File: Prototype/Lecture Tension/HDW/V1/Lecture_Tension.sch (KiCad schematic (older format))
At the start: 5 parts

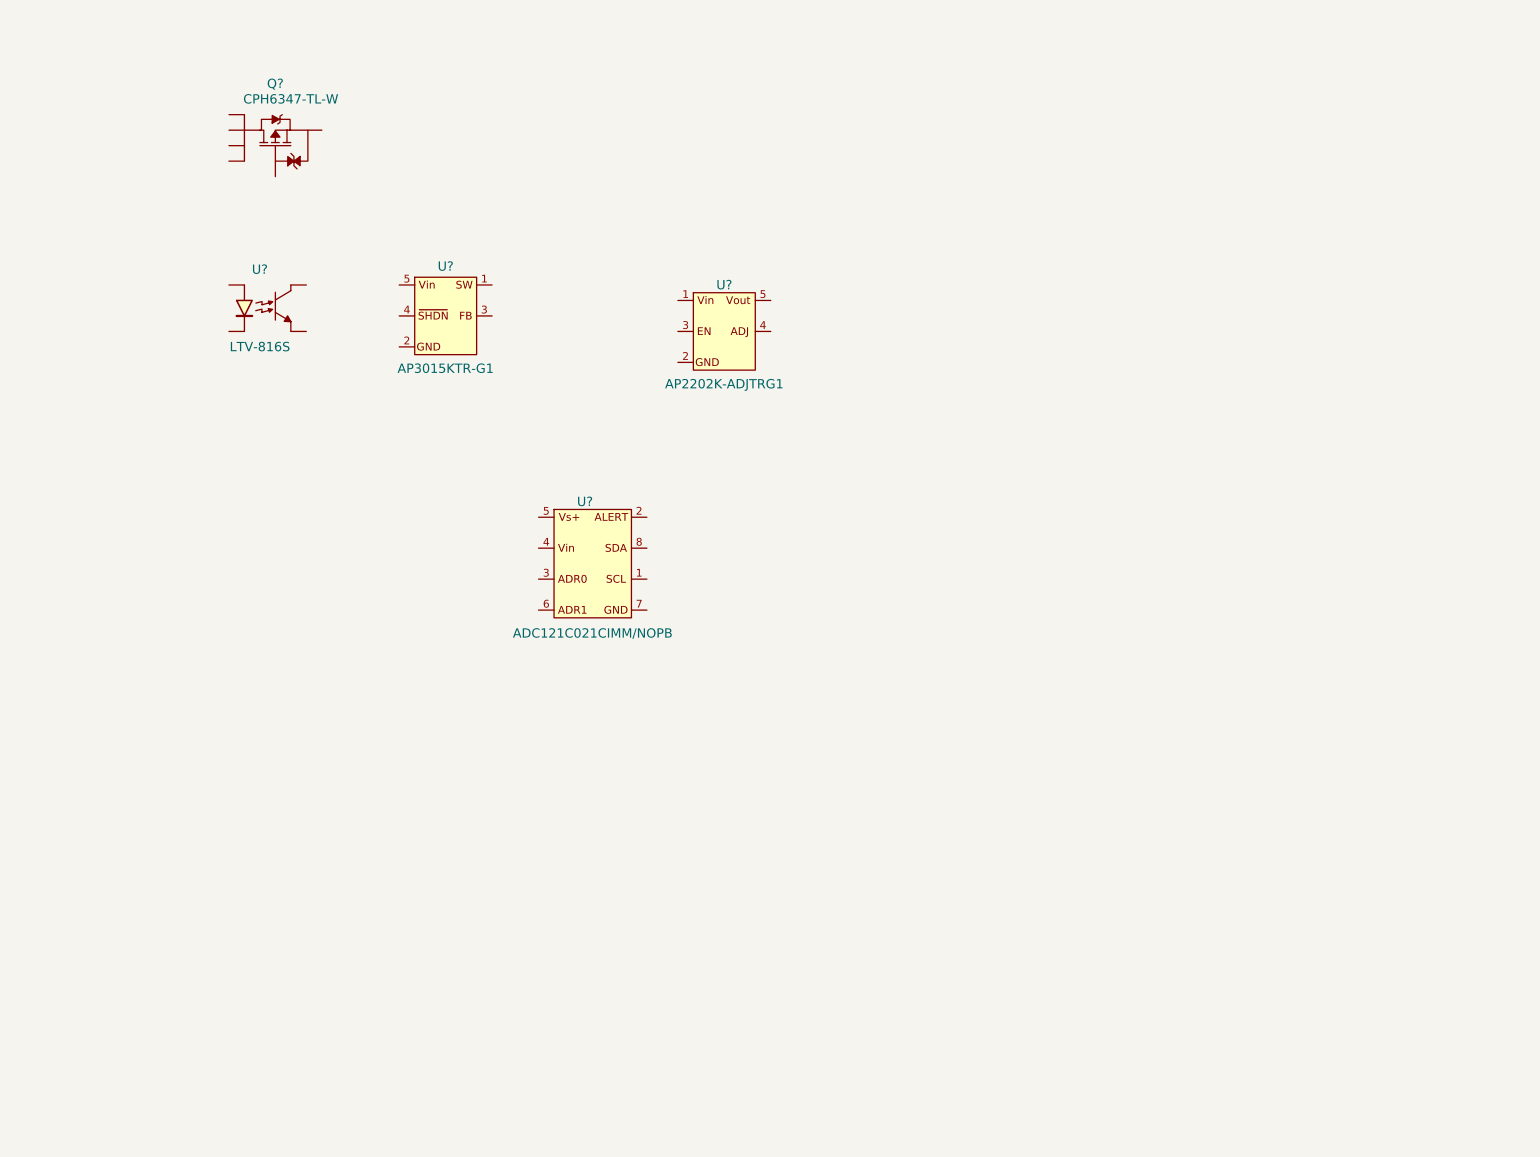
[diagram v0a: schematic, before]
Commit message: SCH ADC part done
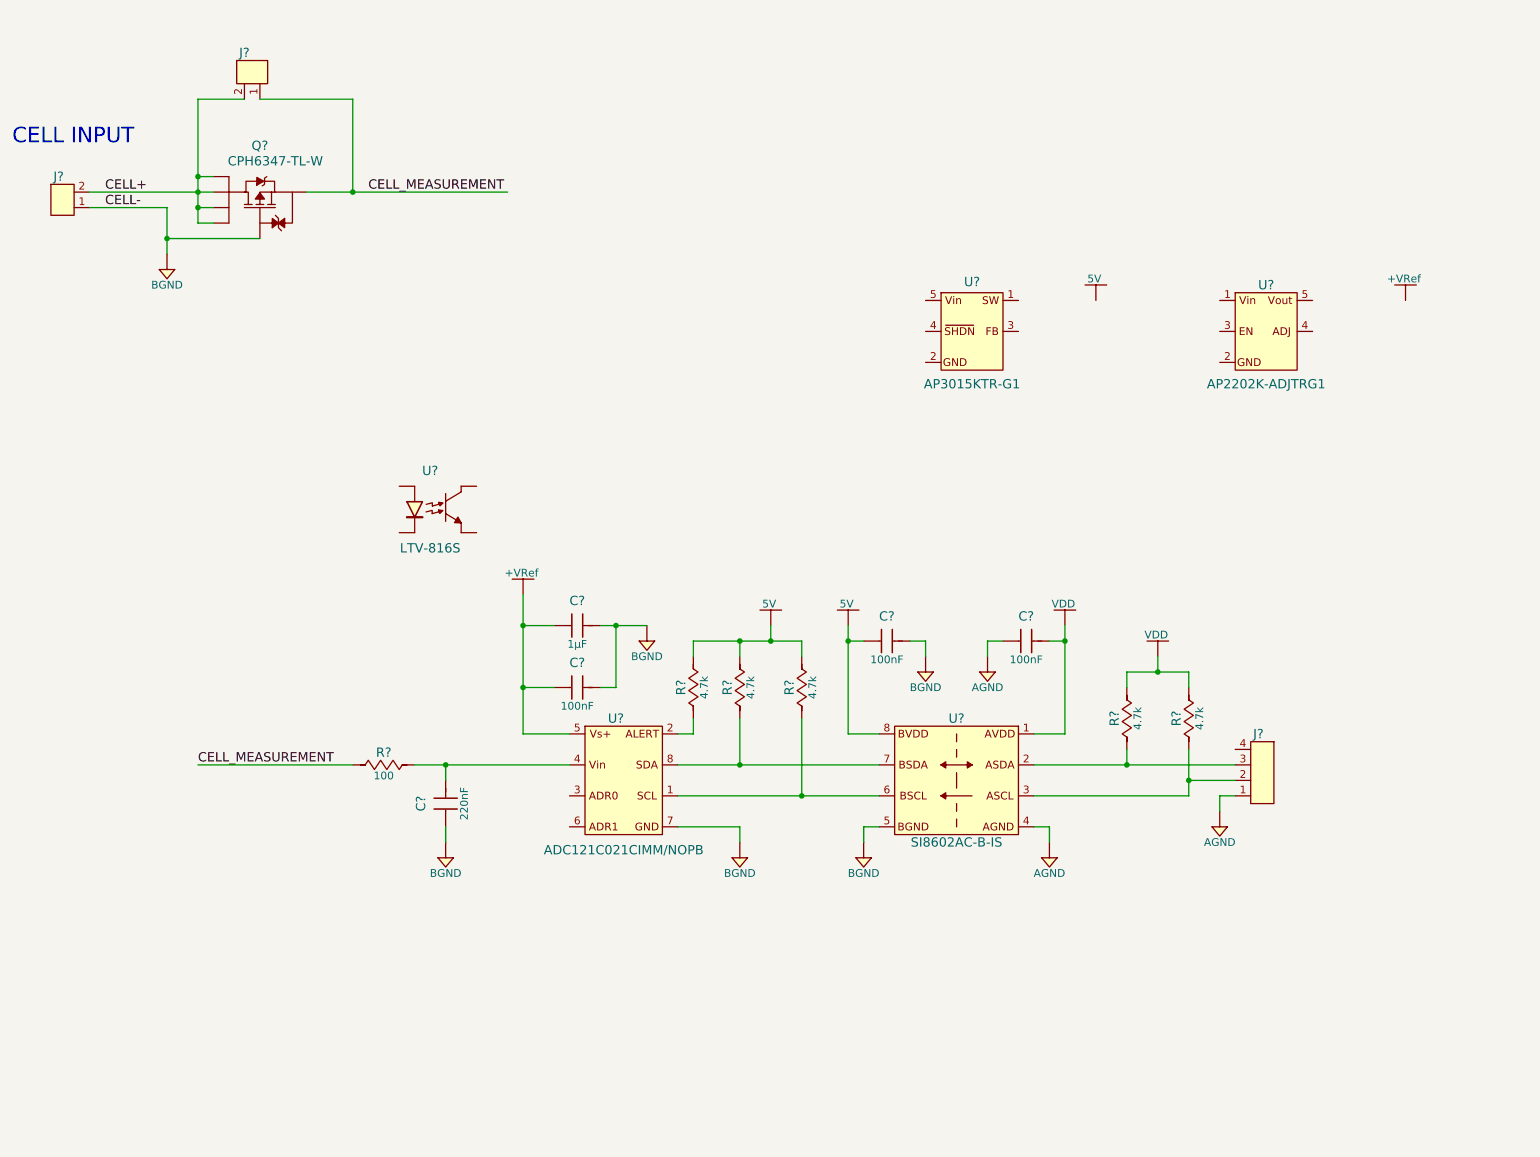
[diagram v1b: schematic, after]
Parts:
- added C? (x3): 885012207098, Capacitors:C0805, symbol 885012207098
- added C?: 885012107015, Capacitors:C0805, symbol 885012107015
- added C?: 885012207047, Capacitors:C0805, symbol 885012207047
- added J?: Header_Male_Pin_2.54mm_1X4_,_Unshrouded, Connectors:Headers_2.54mm_1X4, symbol Header_Male_Pin_2.54mm_1X4_,_Unshrouded
- added J?: 1935161, Connectors:1935161, symbol 1935161
- added J?: Header_Male_Pin_2.54mm_1X2_,_Unshrouded, Connectors:Headers_2.54mm_1X2, symbol Header_Male_Pin_2.54mm_1X2_,_Unshrouded
- added R? (x5): RC0805JR-074K7L, Resistors:R0805, symbol RC0805JR-074K7L
- added R?: RC0805JR-07100RL, Resistors:R0805, symbol RC0805JR-07100RL
- added U?: SI8602AC-B-IS, IC:SOIC-8, symbol SI8602AC-B-IS
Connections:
- net at U?.1 (SCL): now also R?.1, U?.6 (BSCL)
- net at U?.2 (ALERT): now also R?.1
- net at U?.4 (Vin): now also C?.2, R?.2
- net +VRef: now reaches U?.5 (Vs+)
- net +VRef: now also C?.1, C?.1
- net BGND: now reaches U?.7 (GND)
- net BGND: now also Q?.3 (G), C?.1, C?.2, C?.2, C?.2, J?.1, U?.5 (BGND)
- net at U?.8 (SDA): now also R?.1, U?.7 (BSDA)
- net CELL+: now reaches Q?.1 (D)
- net CELL+: now also Q?.2 (D), Q?.5 (D), Q?.6 (D), J?.2, J?.2
- net CELL_MEASUREMENT: now reaches Q?.4 (S)
- net CELL_MEASUREMENT: now also J?.1, R?.1
- new net: J?.2, R?.1, U?.3 (ASCL)
- new net: J?.3, R?.1, U?.2 (ASDA)
- new net 5V: C?.1, R?.2, R?.2, R?.2, U?.8 (BVDD)
- new net AGND: C?.1, J?.1, U?.4 (AGND)
- new net VDD: C?.2, R?.2, R?.2, U?.1 (AVDD)
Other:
- note added: "CELL INPUT"
- moved on the sheet: Q?, U?

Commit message: sch done, need review
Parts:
- added C? (x5): 885012107014, Capacitors:C0805, symbol 885012107014
- added D?: NSR0530HT1G, Diodes:SOD-323, symbol NSR0530HT1G
- added J? (x3): Header_Male_Pin_2.54mm_1X2_,_Unshrouded, Connectors:Headers_2.54mm_1X2, symbol Header_Male_Pin_2.54mm_1X2_,_Unshrouded
- added L?: LQM31PN4R7M00L, Inductors:I1206, symbol LQM31PN4R7M00L
- added L?: LBC3225T101KR, Inductors:LBC3225, symbol LBC3225T101KR
- added R?: RC0805JR-07470KL, Resistors:R0805, symbol RC0805JR-07470KL
- added R?: RC0805JR-0710KL, Resistors:R0805, symbol RC0805JR-0710KL
- added R?: RC0805JR-07330RL, Resistors:R0805, symbol RC0805JR-07330RL
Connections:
- net +VRef: now also J?.1
- net 5V: now also U?.1 (Vin), C?.2, J?.1, R?.1
- net AGND: now also U?.2 (Cathode), J?.1
- net BGND: now also U?.2 (GND), U?.2 (GND), C?.1, C?.1, C?.1, C?.1, C?.1, R?.1
- net CELL_MEASUREMENT: now also U?.4 (C), U?.5 (Vin), C?.2, L?.1, L?.1
- net at U?.1 (SW): now also D?.2 (Anode), L?.2, L?.2
- net at U?.4 (SHDN): now also U?.3 (E), R?.2
- net at U?.3 (EN): now also R?.2
- net at U?.5 (Vout): now also C?.2, J?.2
- net at U?.1 (Anode): now also R?.2
- new net: C?.2, C?.2, D?.1 (Cathode), J?.2
- new net LED_CTRL: J?.2, R?.1
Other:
- note added: "BOOST CTRL\nACTIVE HIGH"
- note added: "ONLY SOLDER ONE"
- moved on the sheet: C?, J?, Q?, R?, U?
